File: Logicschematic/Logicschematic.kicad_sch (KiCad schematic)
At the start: 8 parts, among them K1 Relay_DPDT, SW1 M.B. 6-B, SW2 25c RE, SW3 SW_DPDT_x2, SW4 25c Coin SW, T1 Transformer_1P_2S

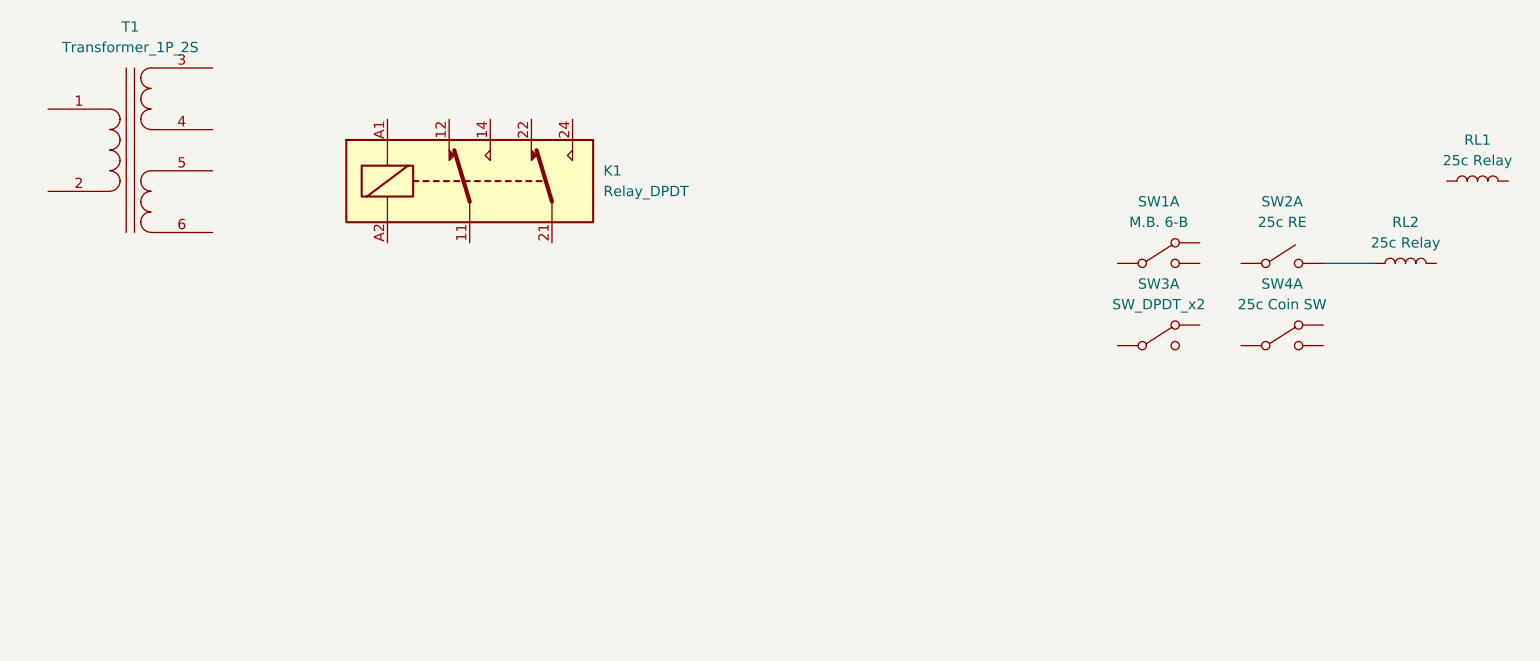
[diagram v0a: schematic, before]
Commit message: Updated software to make the relays, units, etc., from std::map to basic arrays. The individual devices are constants entries in the array. Updated the Schematic with vertical lines to separate the sections. Added the Williams Parts Catalog. Missing important pages in the Instruction Manual.  Need to make a copy of the one in the machine. Updated the Component Index with additional components.
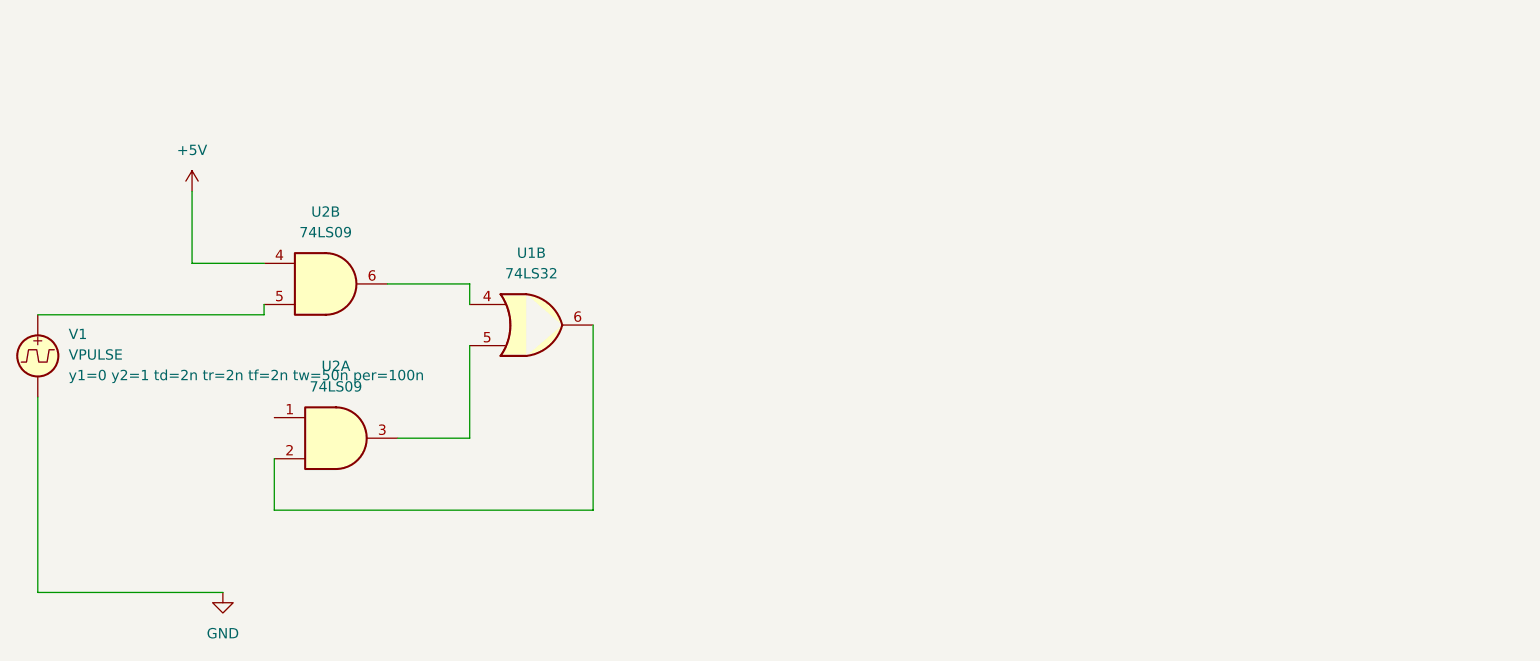
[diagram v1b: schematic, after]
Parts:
- removed K1: Relay_DPDT, symbol Relay:Relay_DPDT
- removed RL1, RL2: 25c Relay, symbol Device:L_Iron
- removed SW1: M.B. 6-B, symbol Switch:SW_DPDT_x2
- removed SW2: 25c RE, symbol Switch:SW_DPDT_x2
- removed SW3: SW_DPDT_x2, symbol Switch:SW_DPDT_x2
- removed SW4: 25c Coin SW, symbol Switch:SW_DPDT_x2
- removed T1: Transformer_1P_2S, symbol Device:Transformer_1P_2S
- added U1: 74LS32, symbol 74xx:74LS32
- added U2: 74LS09, symbol 74xx:74LS09
- added V1: VPULSE, symbol Simulation_SPICE:VPULSE
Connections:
- new net: U2.5, V1.1
- new net: U1.4, U2.6
- new net: U1.6, U2.2
- new net: U1.5, U2.3
- new net +5V: U2.4
- new net GND: V1.2
